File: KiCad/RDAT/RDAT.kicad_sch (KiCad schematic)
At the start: 17 parts

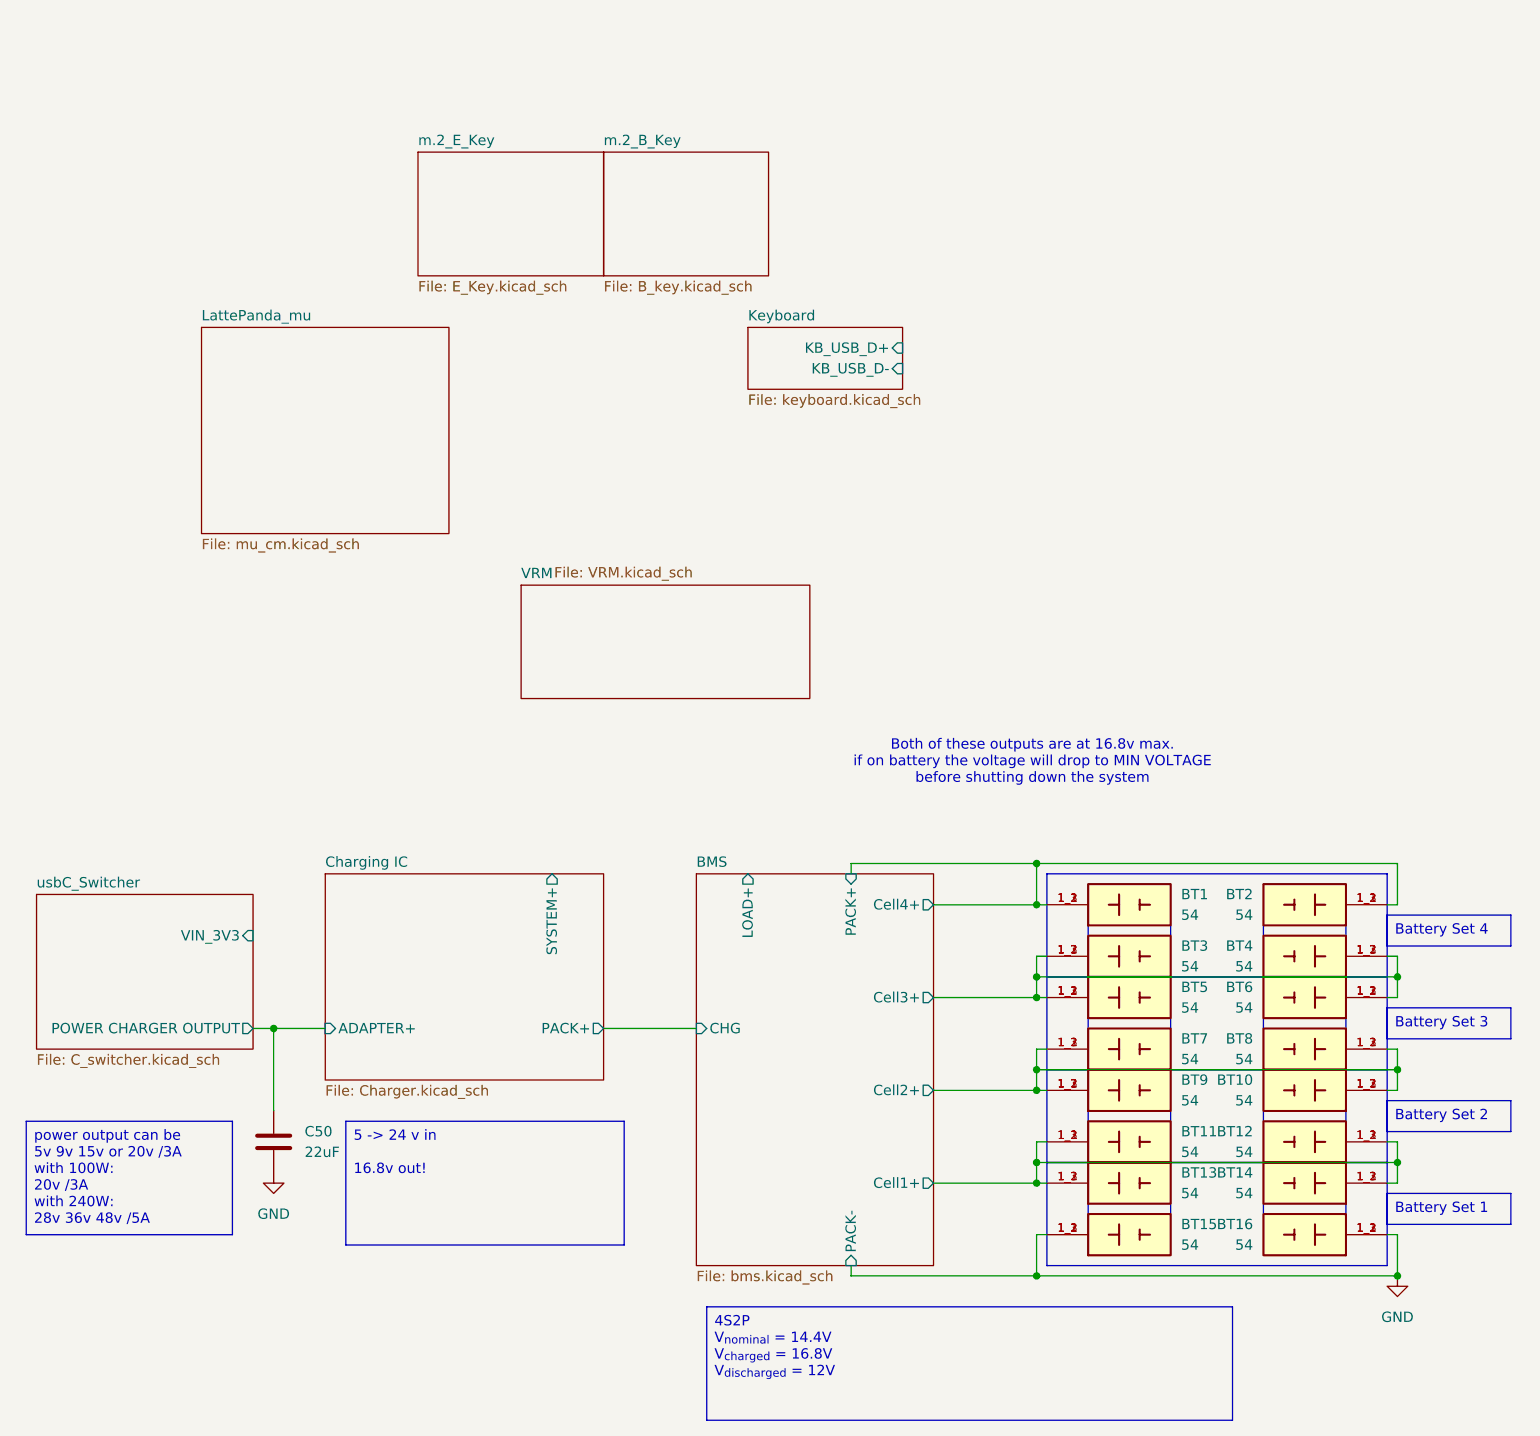
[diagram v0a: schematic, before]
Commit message: Modified Power Stages
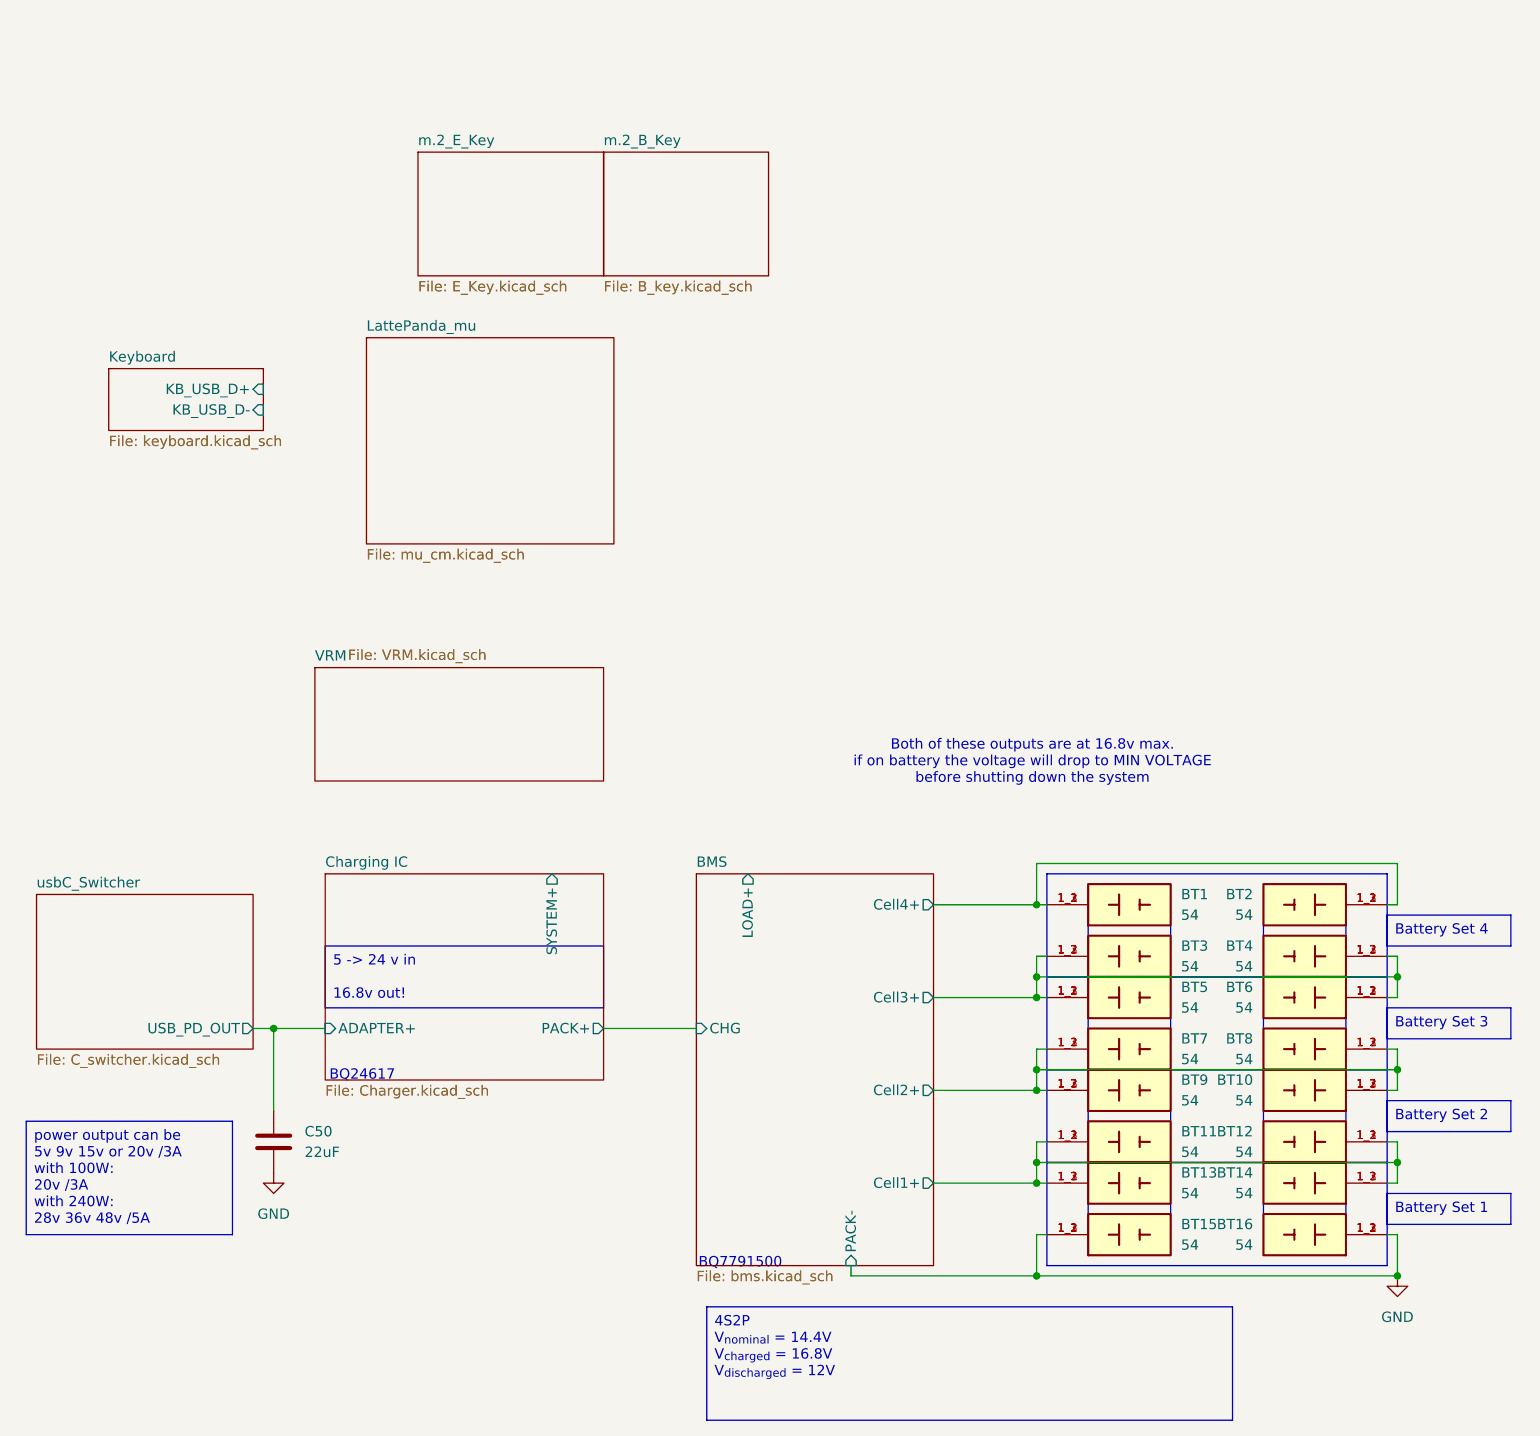
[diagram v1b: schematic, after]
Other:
- sheet BMS ports: added none; removed PACK+
- sheet usbC_Switcher ports: added USB_PD_OUT; removed POWER CHARGER OUTPUT, VIN_3V3
- note added: "BQ24617"
- note added: "BQ7791500"
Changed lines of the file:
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@@
 		)
 	)
+	(text "BQ7791500"
+		(exclude_from_sim no)
+		(at 99.314 166.116 0)
+		(effects
+			(font
+				(size 1.27 1.27)
+			)
+			(justify left)
+		)
+	)
 	(text "Both of these outputs are at 16.8v max.\nif on battery the voltage will drop to MIN VOLTAGE\nbefore shutting down the system\n"
 		(exclude_from_sim no)
@@
 		)
 	)
+	(text "BQ24617"
+		(exclude_from_sim no)
+		(at 53.848 143.002 0)
+		(effects
+			(font
+				(size 1.27 1.27)
+			)
+			(justify left)
+		)
+	)
 	(text_box "Battery Set 2\n"
 		(exclude_from_sim no)
@@
 	(text_box "5 -> 24 v in\n\n16.8v out!\n"
 		(exclude_from_sim no)
-		(at 55.88 148.59 0)
-		(size 34.29 15.24)
+		(at 53.34 127 0)
+		(size 34.29 7.62)
 		(margins 0.9525 0.9525 0.9525 0.9525)
 		(stroke
@@
 	)
 	(junction
-		(at 140.97 116.84)
-		(diameter 0)
-		(color 0 0 0 0)
-	)
-	(junction
 		(at 140.97 167.64)
 		(diameter 0)
@@
 	(wire
 		(pts
-			(xy 118.11 116.84) (xy 118.11 118.11)
-		)
-		(stroke
-			(width 0)
-			(type default)
-		)
-	)
-	(wire
-		(pts
 			(xy 140.97 167.64) (xy 140.97 162.56)
 		)
@@
 	(wire
 		(pts
-			(xy 87.63 137.16) (xy 99.06 137.16)
-		)
-		(stroke
-			(width 0)
-			(type default)
-		)
-	)
-	(wire
-		(pts
 			(xy 184.15 128.27) (xy 185.42 128.27)
 		)
@@
 	(wire
 		(pts
-			(xy 118.11 116.84) (xy 140.97 116.84)
+			(xy 44.45 137.16) (xy 46.99 137.16)
 		)
 		(stroke
@@
 	(wire
 		(pts
-			(xy 44.45 137.16) (xy 46.99 137.16)
+			(xy 87.63 137.16) (xy 99.06 137.16)
 		)
 		(stroke
@@
 	)
 	(sheet
-		(at 105.41 50.8)
+		(at 26.67 55.88)
 		(size 19.05 7.62)
 		(exclude_from_sim no)
@@
 		)
 		(property "Sheetname" "Keyboard"
-			(at 105.41 50.0884 0)
+			(at 26.67 55.1684 0)
 			(effects
 				(font
@@
 		)
 		(property "Sheetfile" "keyboard.kicad_sch"
-			(at 105.41 59.0046 0)
+			(at 26.67 64.0846 0)
 			(effects
 				(font
@@
 		)
 		(pin "KB_USB_D-" input
-			(at 124.46 55.88 0)
+			(at 45.72 60.96 0)
 			(effects
 				(font
@@
 		)
 		(pin "KB_USB_D+" input
-			(at 124.46 53.34 0)
+			(at 45.72 58.42 0)
 			(effects
 				(font
@@
 			)
 		)
-		(pin "POWER CHARGER OUTPUT" output
+		(pin "USB_PD_OUT" output
 			(at 44.45 137.16 0)
 			(effects
@@
 			)
 		)
-		(pin "VIN_3V3" input
-			(at 44.45 125.73 0)
-			(effects
-				(font
-					(size 1.27 1.27)
-				)
-				(justify right)
-			)
-		)
 		(instances
 			(project "RDAT"
@@
 	)
 	(sheet
-		(at 38.1 50.8)
+		(at 58.42 52.07)
 		(size 30.48 25.4)
 		(exclude_from_sim no)
@@
 		)
 		(property "Sheetname" "LattePanda_mu"
-			(at 38.1 50.0884 0)
+			(at 58.42 51.3584 0)
 			(effects
 				(font
@@
 		)
 		(property "Sheetfile" "mu_cm.kicad_sch"
-			(at 38.1 76.7846 0)
+			(at 58.42 78.0546 0)
 			(effects
 				(font
@@
 	)
 	(sheet
-		(at 77.47 82.55)
+		(at 52.07 92.71)
 		(size 35.56 13.97)
 		(exclude_from_sim no)
@@
 		)
 		(property "Sheetname" "VRM"
-			(at 77.47 81.8384 0)
+			(at 52.07 91.9984 0)
 			(effects
 				(font
@@
 		)
 		(property "Sheetfile" "VRM.kicad_sch"
-			(at 81.534 80.264 0)
+			(at 56.134 90.424 0)
 			(effects
 				(font
@@
 			)
 		)
-		(pin "PACK+" input
-			(at 118.11 118.11 90)
-			(effects
-				(font
-					(size 1.27 1.27)
-				)
-				(justify right)
-			)
-		)

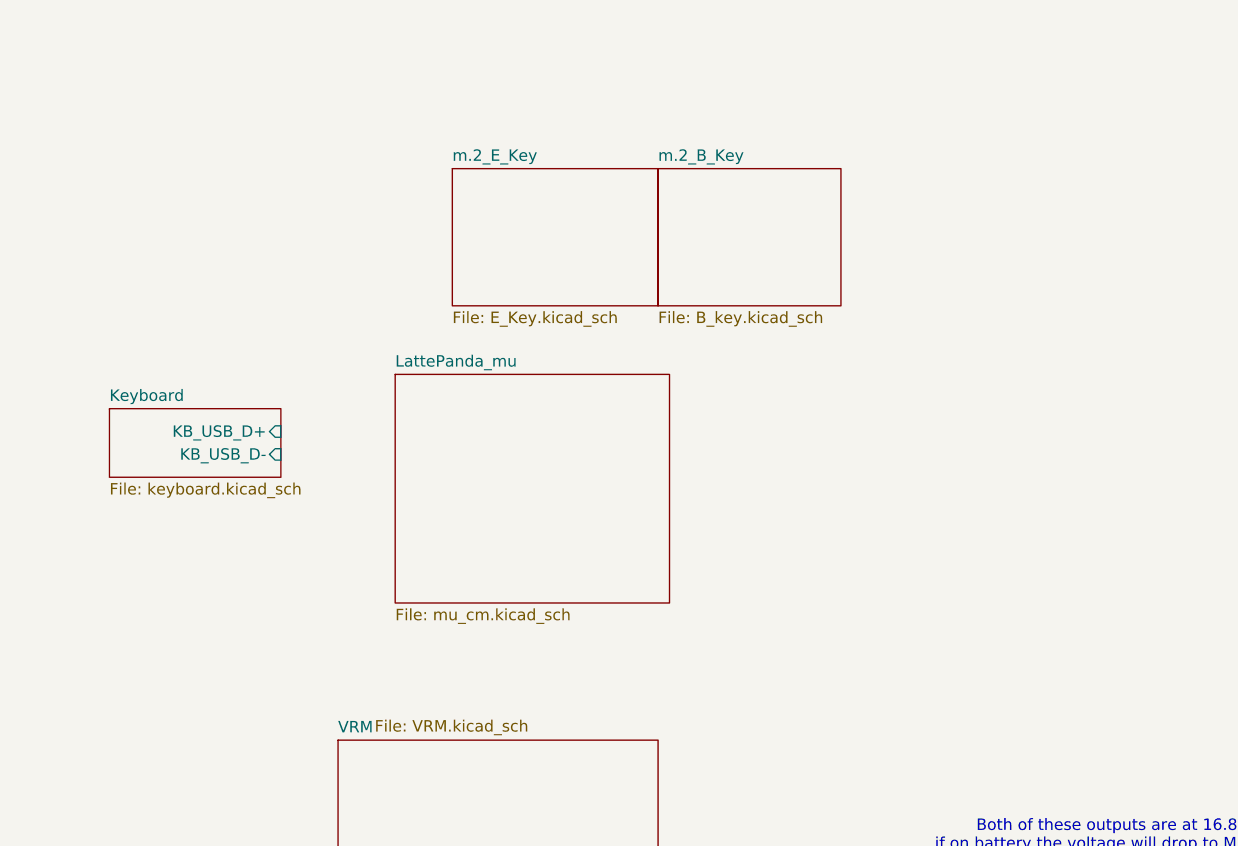
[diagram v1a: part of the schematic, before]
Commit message: Connected m.2 E Key
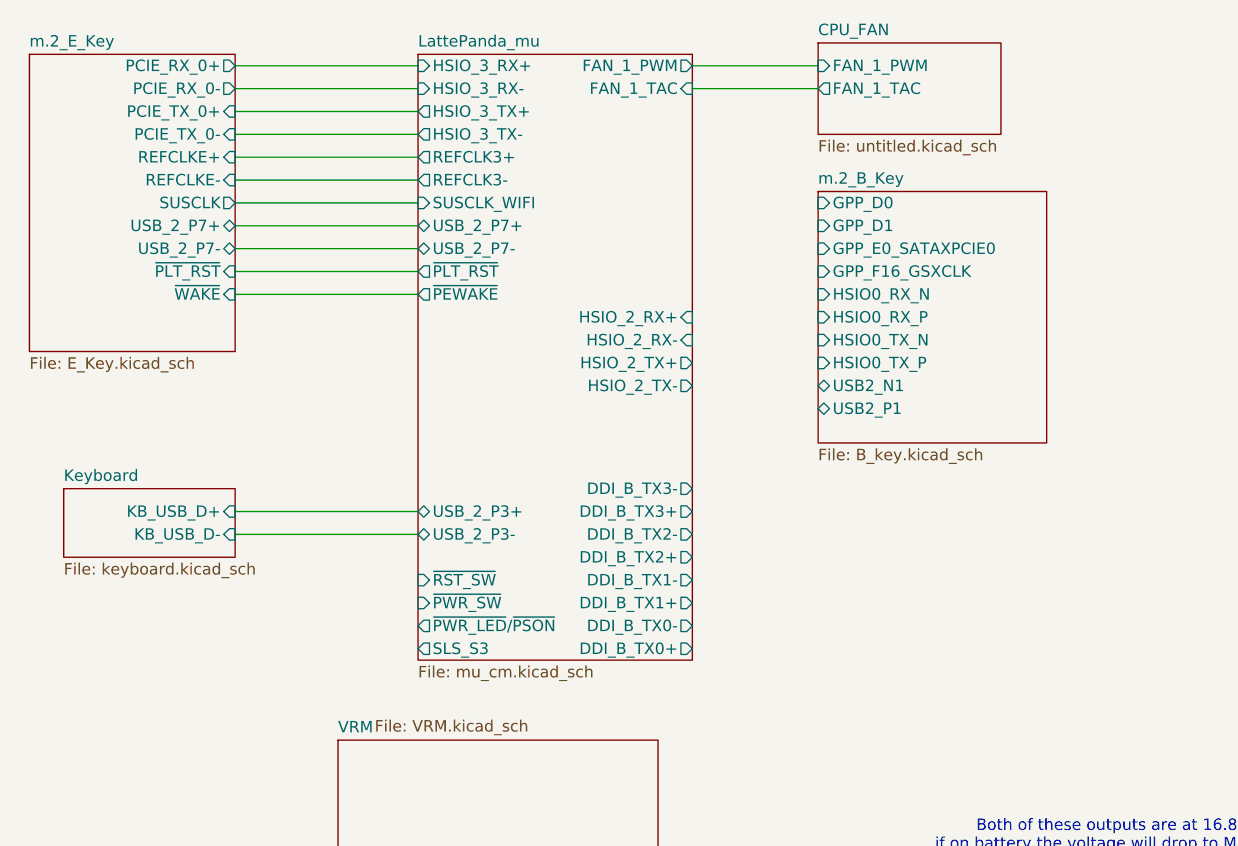
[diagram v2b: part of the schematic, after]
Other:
- added sheet CPU_FAN (untitled.kicad_sch)
- sheet LattePanda_mu ports: added DDI_B_TX0+, DDI_B_TX0-, DDI_B_TX1+, DDI_B_TX1-, DDI_B_TX2+, DDI_B_TX2-, DDI_B_TX3+, DDI_B_TX3-, FAN_1_PWM, FAN_1_TAC, HSIO_2_RX+, HSIO_2_RX-, HSIO_2_TX+, HSIO_2_TX-, HSIO_3_RX+, HSIO_3_RX-, HSIO_3_TX+, HSIO_3_TX-, REFCLK3+, REFCLK3-, SLS_S3, SUSCLK_WIFI, USB_2_P3+, USB_2_P3-, USB_2_P7+, USB_2_P7-, ~{PEWAKE}, ~{PLT_RST}, ~{PWR_LED}/~{PSON}, ~{PWR_SW}, ~{RST_SW}; removed none
- sheet m.2_B_Key ports: added GPP_D0, GPP_D1, GPP_E0_SATAXPCIE0, GPP_F16_GSXCLK, HSIO0_RX_N, HSIO0_RX_P, HSIO0_TX_N, HSIO0_TX_P, USB2_N1, USB2_P1; removed none
- sheet m.2_E_Key ports: added PCIE_RX_0+, PCIE_RX_0-, PCIE_TX_0+, PCIE_TX_0-, REFCLKE+, REFCLKE-, SUSCLK, USB_2_P7+, USB_2_P7-, ~{PLT_RST}, ~{WAKE}; removed none
